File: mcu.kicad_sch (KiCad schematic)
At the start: 0 parts

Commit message: added power schematic
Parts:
- added U1: STM32F469AEHx, Package_BGA:UFBGA-169_7x7mm_Layout13x13_P0.5mm, symbol MCU_ST_STM32F4:STM32F469AEHx
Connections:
- new net: U1.D11 (VSS), U1.E3 (VSS), U1.F5 (VSS), U1.F8 (VSS), U1.G7 (VSS), U1.G9 (VSS), U1.J1 (VSS), U1.J10 (VSS), U1.J6 (VSS), U1.J7 (VSS), U1.M9 (VSS)
- new net: U1.H11 (VSSDSI), U1.K11 (VSSDSI)

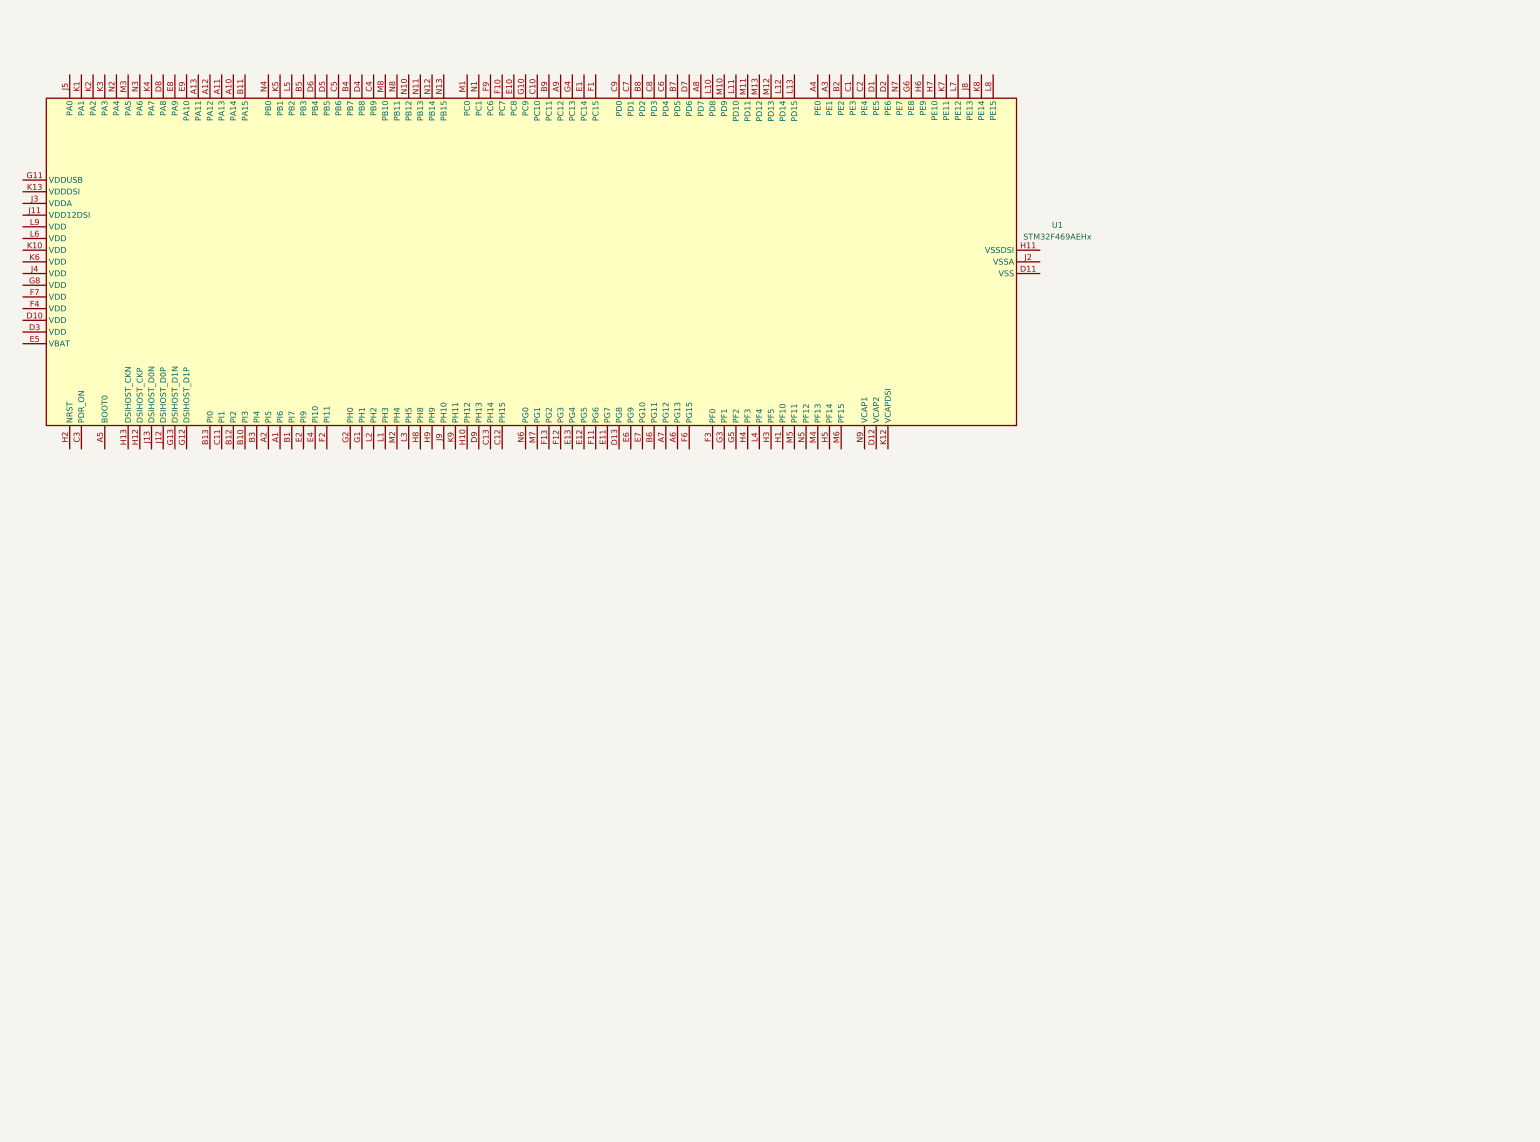
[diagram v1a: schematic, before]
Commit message: added mcu and SWD connector
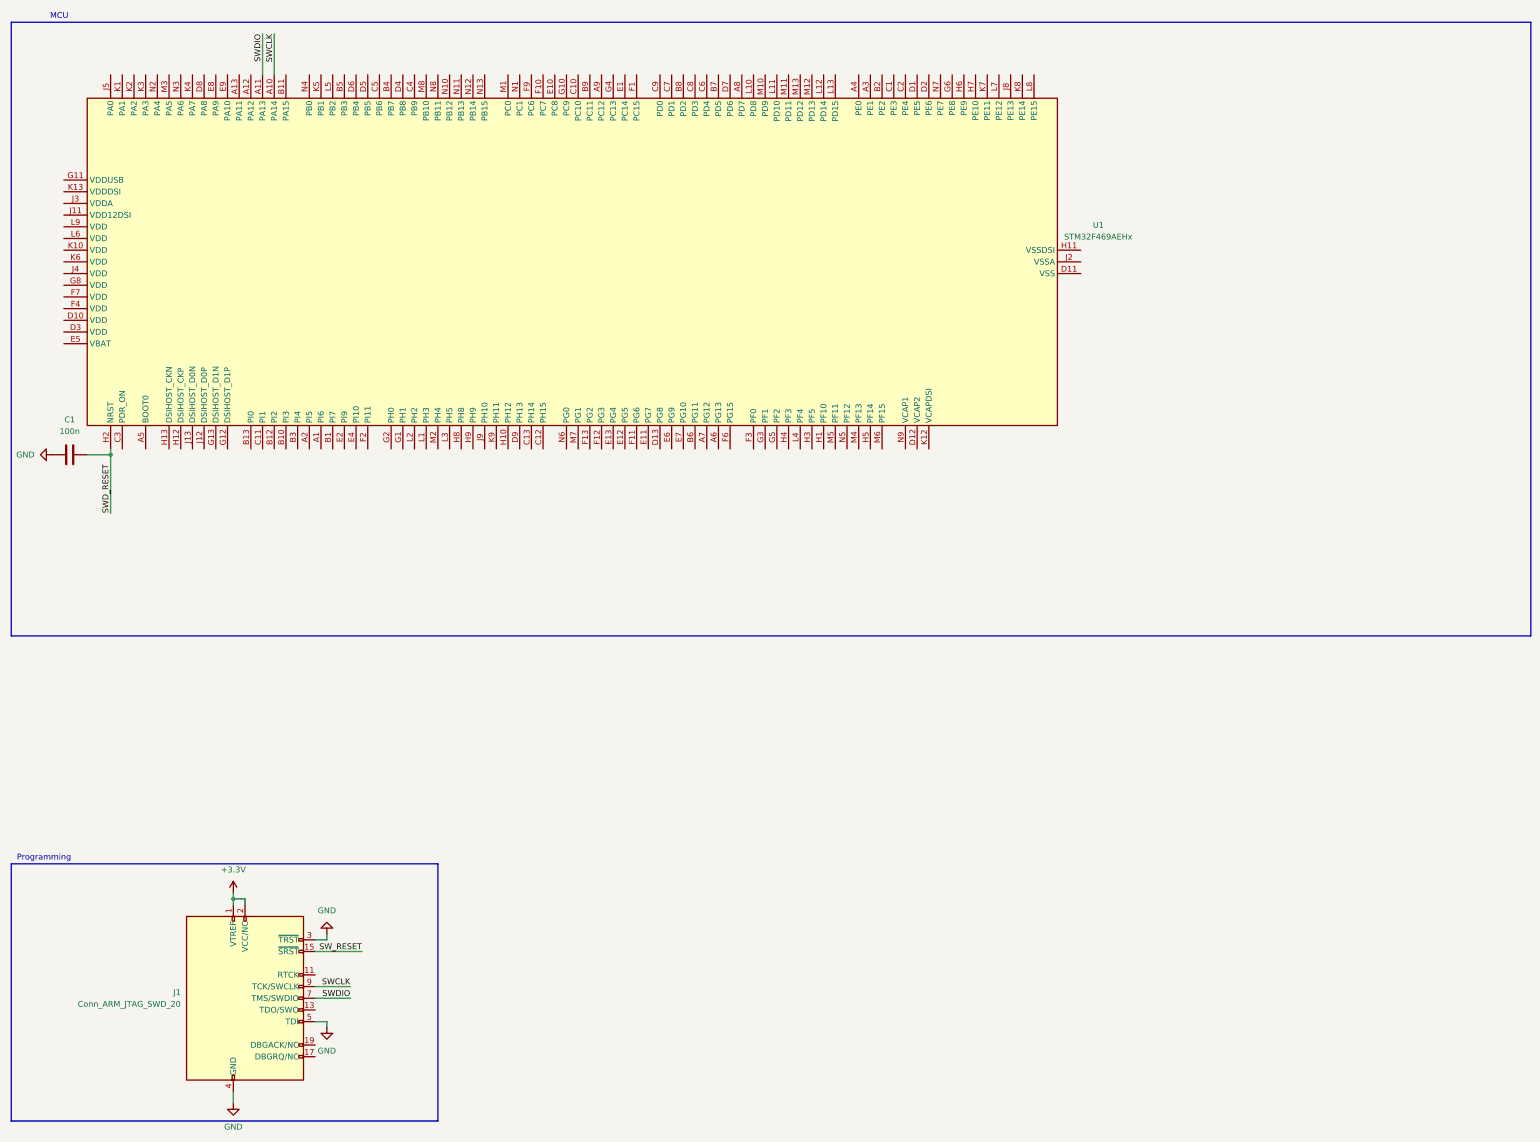
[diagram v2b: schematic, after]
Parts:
- added C1: 100n, symbol Device:C
- added J1: Conn_ARM_JTAG_SWD_20, symbol Connector:Conn_ARM_JTAG_SWD_20
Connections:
- net SWCLK: now reaches U1.A10 (PA14)
- net SWCLK: now also J1.9 (TCK/SWCLK)
- net SWDIO: now reaches U1.A11 (PA13)
- net SWDIO: now also J1.7 (TMS/SWDIO)
- net SWD_RESET: now reaches U1.H2 (NRST)
- net SWD_RESET: now also C1.2
- new net +3.3V: J1.1 (VTREF), J1.2 (VCC/NC)
- new net GND: C1.1, J1.10 (GND), J1.12 (GND), J1.14 (GND), J1.16 (GND), J1.18 (GND), J1.20 (GND), J1.3 (~{TRST}), J1.4 (GND), J1.5 (TDI), J1.6 (GND), J1.8 (GND)
- new net SW_RESET: J1.15 (~{SRST})
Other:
- note added: "MCU"
- note added: "Programming"
- moved on the sheet: U1

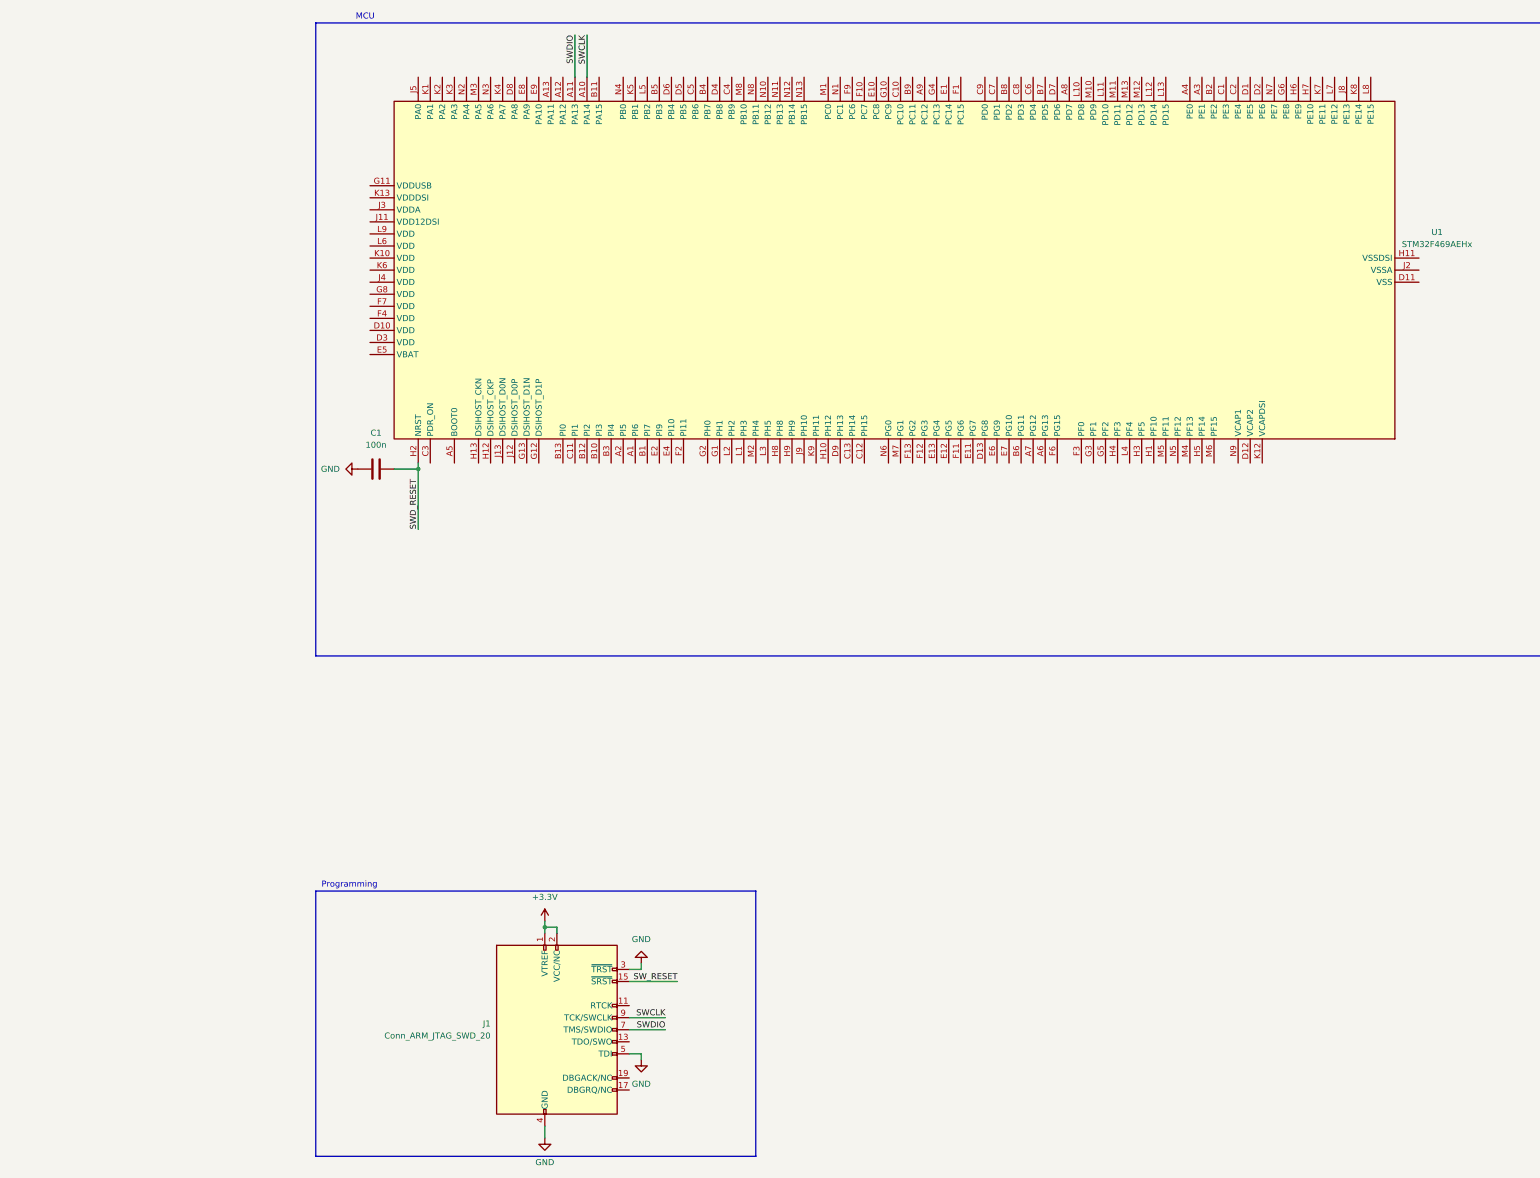
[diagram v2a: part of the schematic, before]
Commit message: changed mcu and added power
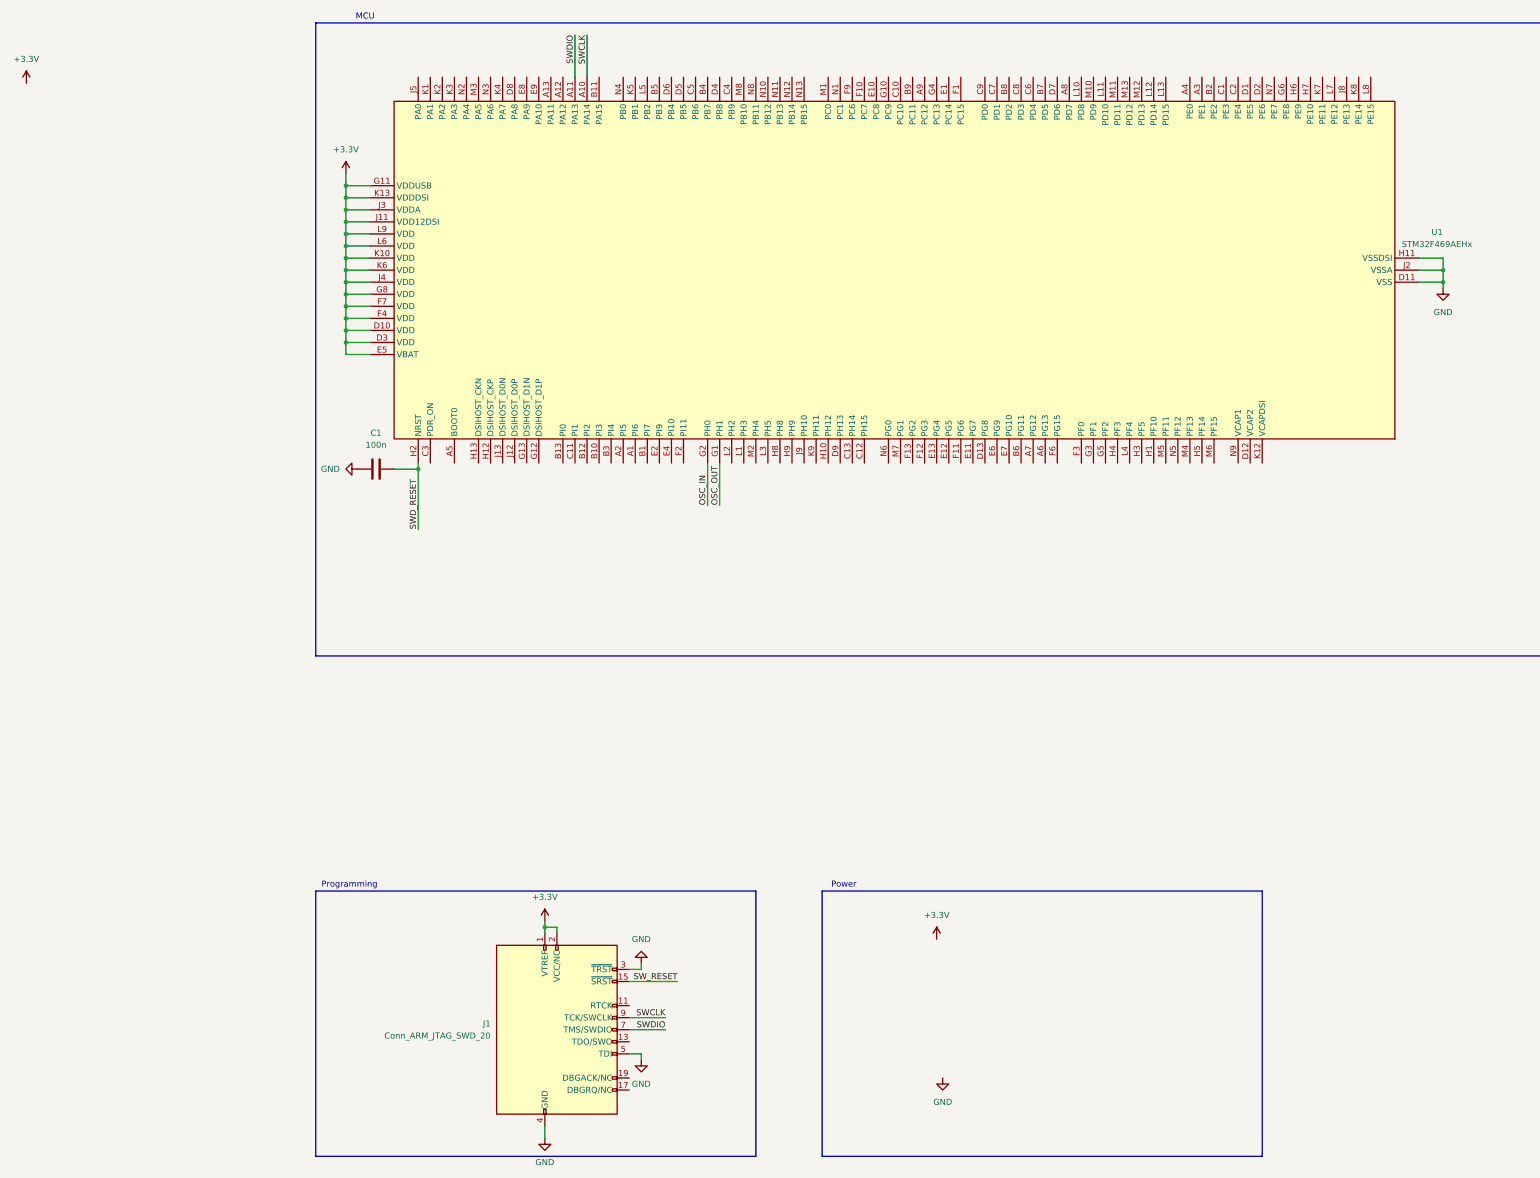
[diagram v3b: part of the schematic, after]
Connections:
- net +3.3V: now also U1.D10 (VDD), U1.D3 (VDD), U1.E5 (VBAT), U1.F4 (VDD), U1.F7 (VDD), U1.G11 (VDDUSB), U1.G8 (VDD), U1.J11 (VDD12DSI), U1.J3 (VDDA), U1.J4 (VDD), U1.K10 (VDD), U1.K13 (VDDDSI), U1.K6 (VDD), U1.L6 (VDD), U1.L9 (VDD)
- net GND: now also U1.D11 (VSS), U1.E3 (VSS), U1.F5 (VSS), U1.F8 (VSS), U1.G7 (VSS), U1.G9 (VSS), U1.H11 (VSSDSI), U1.J1 (VSS), U1.J10 (VSS), U1.J2 (VSSA), U1.J6 (VSS), U1.J7 (VSS), U1.K11 (VSSDSI), U1.M9 (VSS)
- net OSC_OUT: now reaches U1.G1 (PH1)
- net OSC_IN: now reaches U1.G2 (PH0)
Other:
- note added: "Power"
